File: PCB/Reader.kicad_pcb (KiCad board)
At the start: 2 copper layers, 40.4 x 60 mm, 42 parts, among them J1 Conn_01x04, J2 Amphenol Dubox ‎76383-402LF‎, J3 Conn_01x04, J4 Conn_01x08, J5 Conn_01x10, J6 Conn_01x03, J7 Conn_01x02, Q1 2N7002, Q2 2N7002, Q3 2N7002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

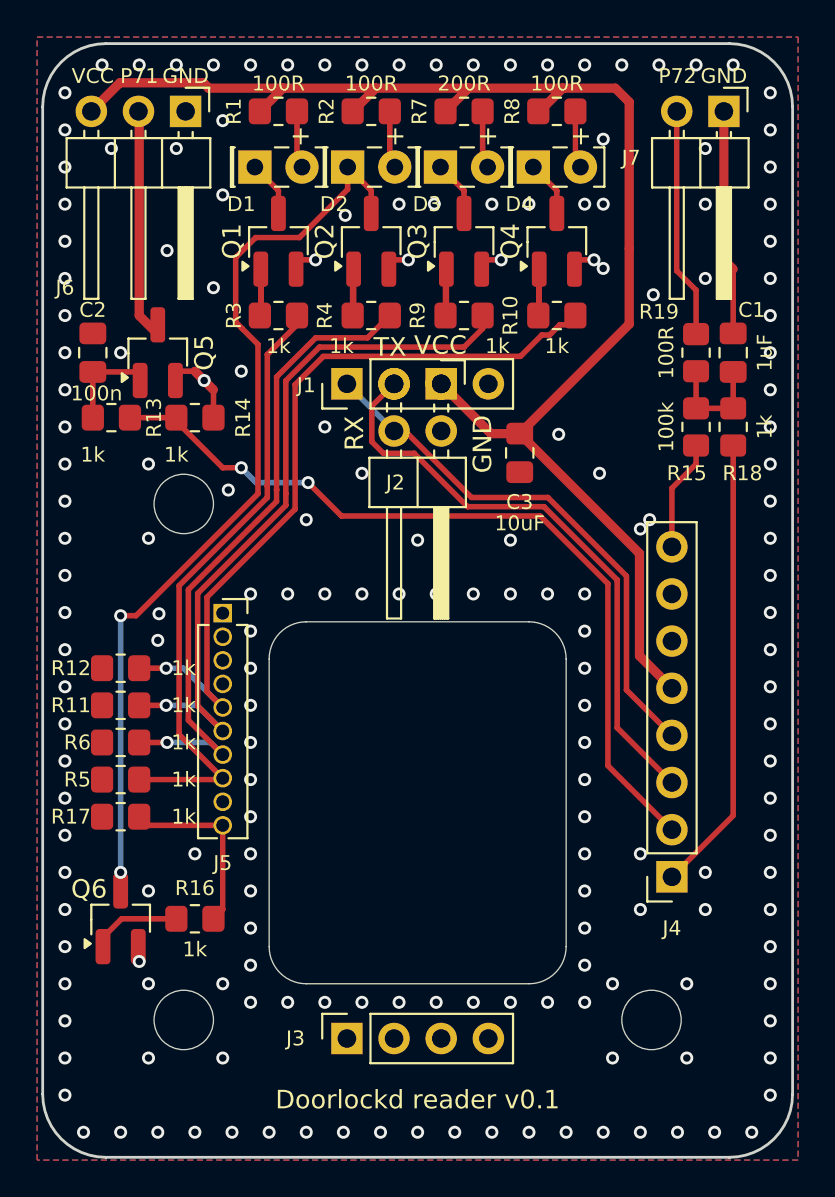
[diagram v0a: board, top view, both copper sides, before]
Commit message: Small layout and via improvements
This also makes some changes that are likely because of using a slightly
newer KiCad version.
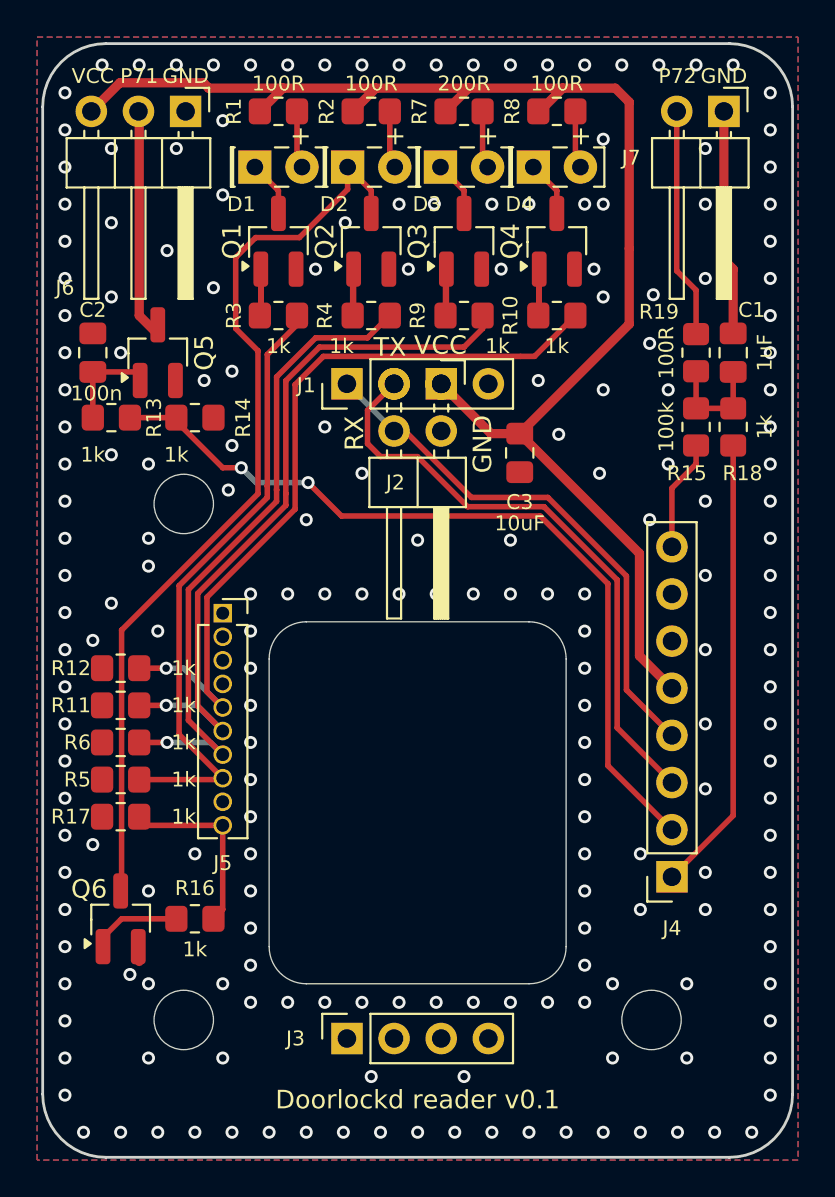
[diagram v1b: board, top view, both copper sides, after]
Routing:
- net GND: track 21.7 -> 13.5 mm, vias 188 -> 206
- net Net-(D2-K): track 51.0 -> 50.0 mm, vias 2 -> 0

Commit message: Improve revision silk and re-add OSHW logo
The logo got removed at some point, so re-add it.

Remove the PCB name on the front in favor of the silk on the back where
there is more room.

Match the PCB name to the git repo name, and auto-fill the board
revision.
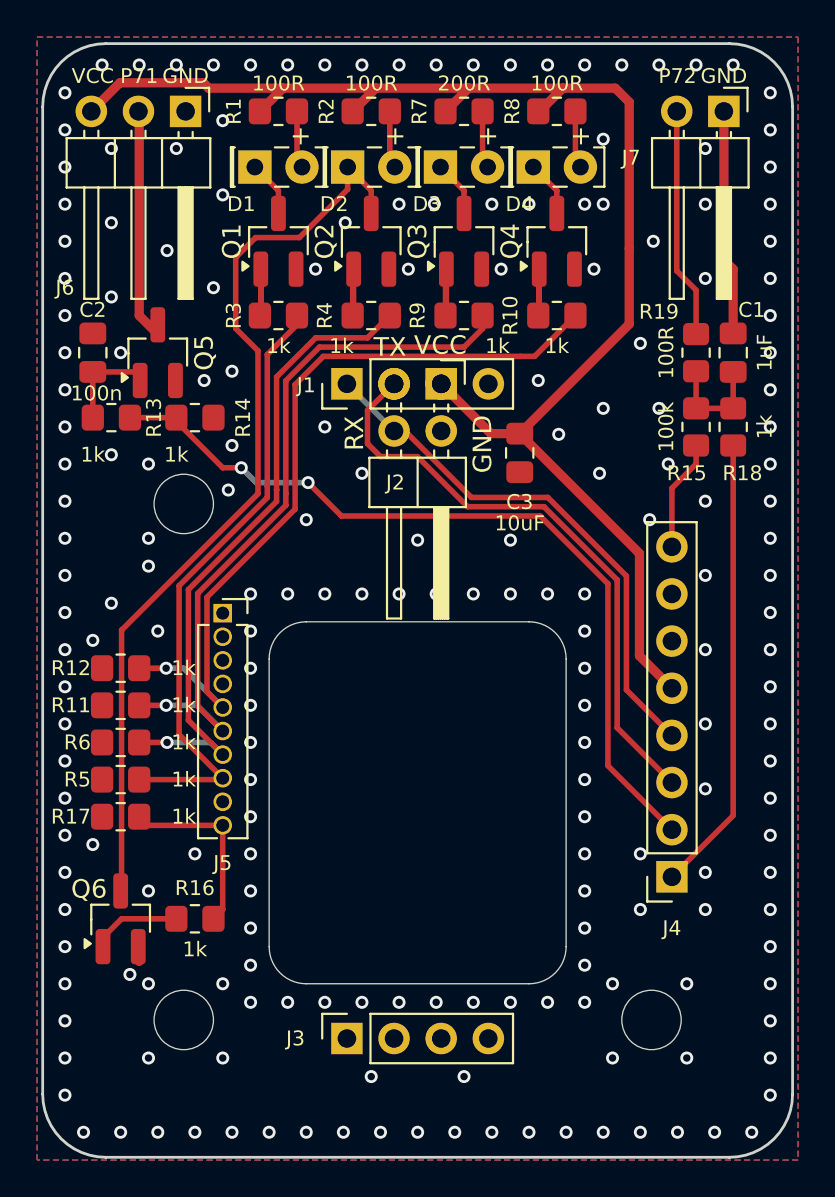
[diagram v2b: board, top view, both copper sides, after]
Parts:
- added LOGO1: Logo_Open_Hardware_Large, Symbol:OSHW-Symbol_8.9x8mm_SilkScreen, B.Cu at (112.0, 77.0)
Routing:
- net GND: vias 206 -> 205
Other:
- board text added: "doorlockd-PCB-Reader"
- board text added: "rev ${BOARD_REVISION}"
- board text removed: "Doorlockd reader v0.1"
- board text removed: "Doorlockd-reader"
- board text removed: "v0.1"

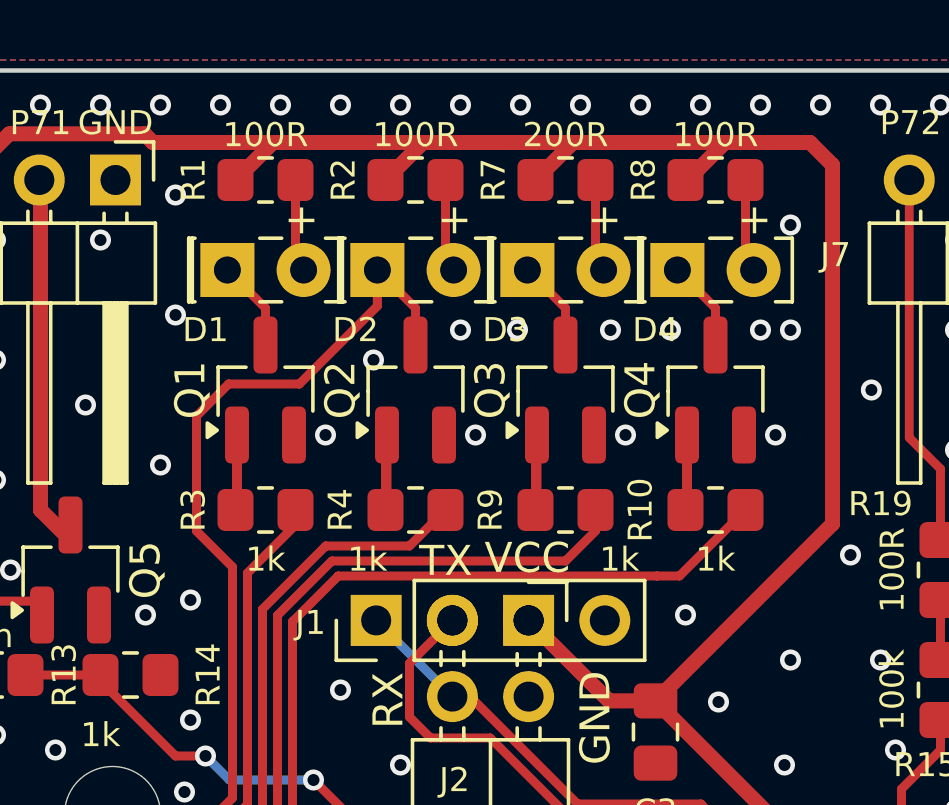
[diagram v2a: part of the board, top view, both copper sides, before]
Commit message: Replace LED resistor values with lookup table
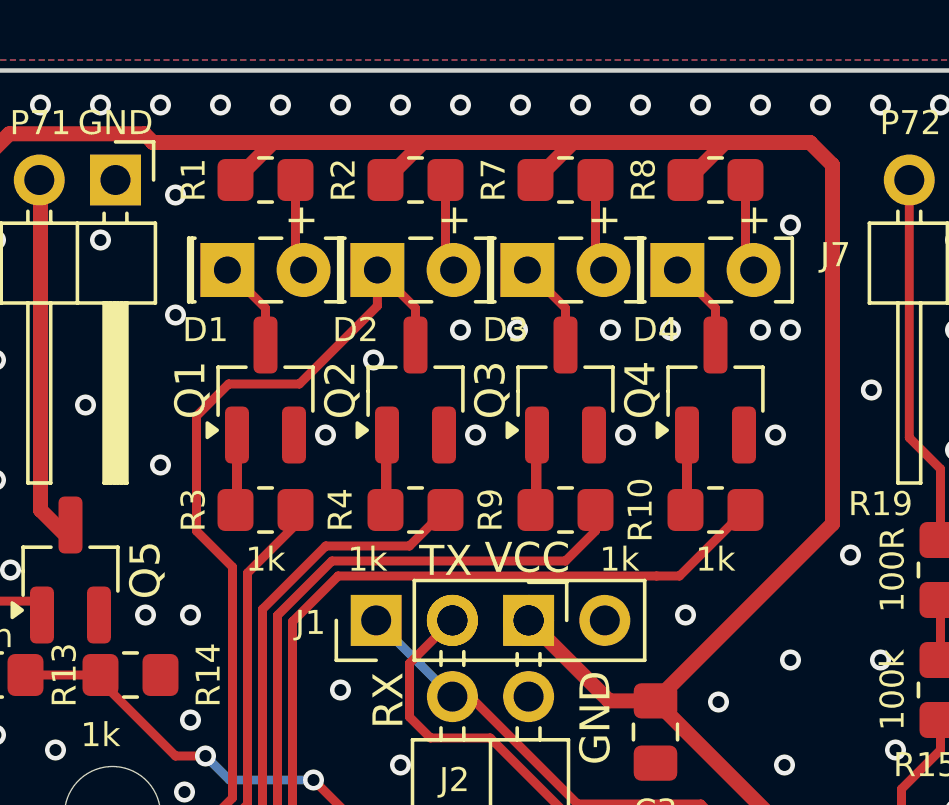
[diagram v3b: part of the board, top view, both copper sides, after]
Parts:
- R1, R2, R8: value 100R -> ~
- R7: value 200R -> ~
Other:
- board text added: "LED resistors Yellow: 100R Green: 100R Red: 200R"
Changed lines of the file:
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@@
 			)
 		)
-		(property "Value" "200R"
+		(property "Value" "~"
 			(at 0 -1.5 0)
 			(layer "F.Fab")
@@
 			(at 0 -1.5 0)
 			(layer "F.SilkS")
+			(hide yes)
 			(effects
 				(font
@@
 			)
 		)
-		(property "Value" "100R"
+		(property "Value" "~"
 			(at 0 -1.5 0)
 			(layer "F.Fab")
@@
 			(at 0 -1.5 0)
 			(layer "F.SilkS")
+			(hide yes)
 			(effects
 				(font
@@
 			)
 		)
-		(property "Value" "100R"
+		(property "Value" "~"
 			(at 0 -1.5 0)
 			(layer "F.Fab")
@@
 			(at 0 -1.5 0)
 			(layer "F.SilkS")
+			(hide yes)
 			(effects
 				(font
@@
 			)
 		)
-		(property "Value" "100R"
+		(property "Value" "~"
 			(at 0 -1.5 0)
 			(layer "F.Fab")
@@
 			(at 0 -1.5 0)
 			(layer "F.SilkS")
+			(hide yes)
 			(effects
 				(font
@@
 		)
 	)
+	(gr_rect
+		(start 83.5 74)
+		(end 92.5 80)
+		(stroke
+			(width 0.15)
+			(type default)
+		)
+		(fill none)
+		(layer "B.SilkS")
+	)
 	(gr_line
 		(start 79.8 82.05)
@@
 		)
 	)
+	(gr_text "LED resistors\nYellow: 100R\nGreen: 100R\nRed: 200R"
+		(at 88 77 0)
+		(layer "B.SilkS")
+		(effects
+			(font
+				(size 0.8 0.8)
+				(thickness 0.1)
+			)
+			(justify mirror)
+		)
+	)
 	(gr_text "rev ${BOARD_REVISION}"
 		(at 100 73.5 0)
@@
 	)
 	(via
-		(at 90 79)
+		(at 90 79.5)
 		(size 0.7)
 		(drill 0.4)
